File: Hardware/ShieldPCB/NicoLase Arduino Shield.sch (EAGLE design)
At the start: 19 parts, among them IC1 4050D, J1 ARDUINO_R3_SHIELD, U1 7432SE

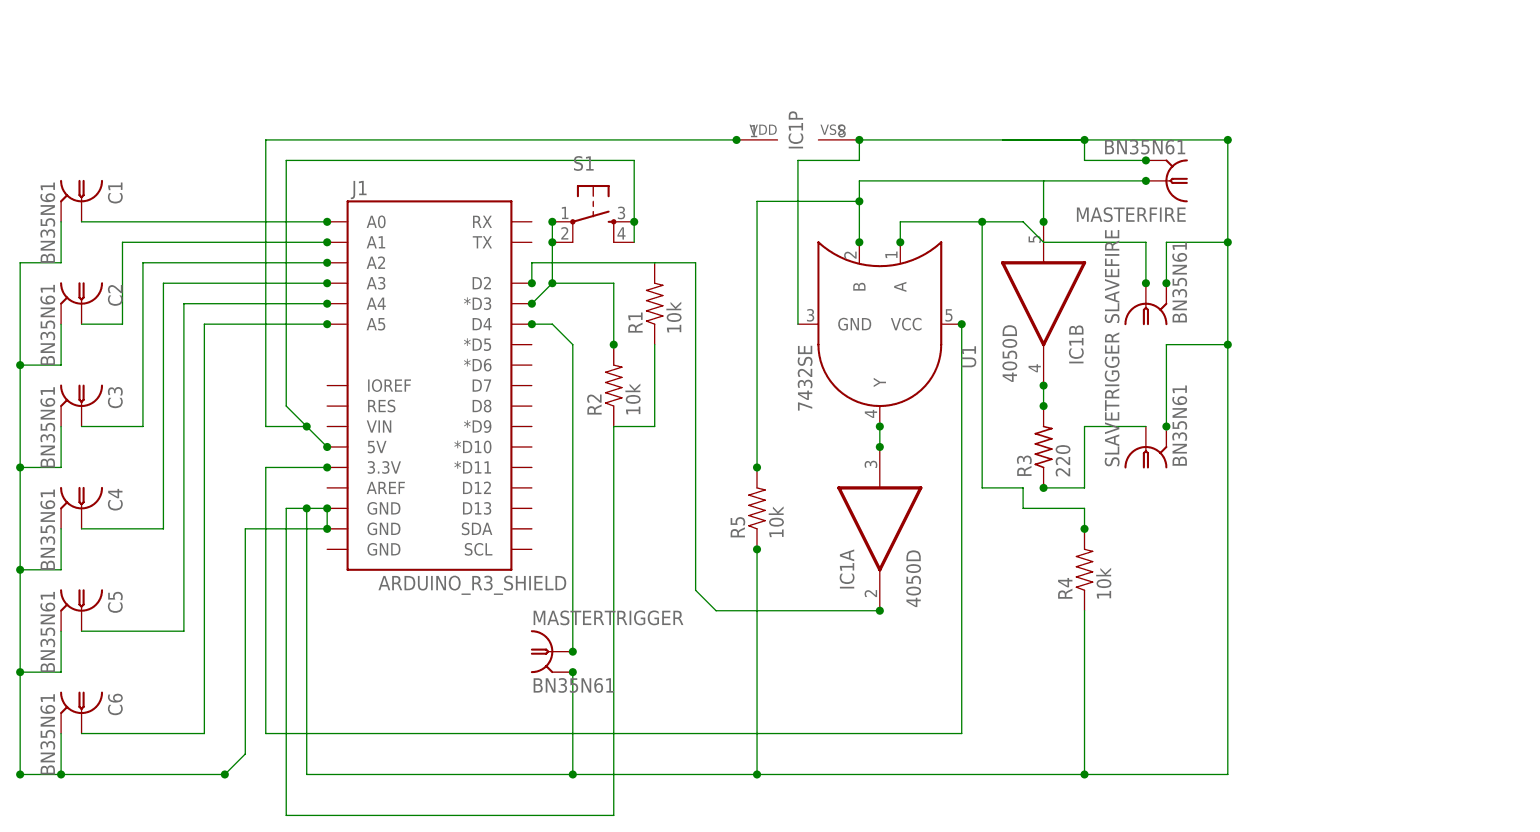
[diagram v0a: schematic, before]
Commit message: Added 0.1uF capacitors on power rails. Correcter minor schematic issues.
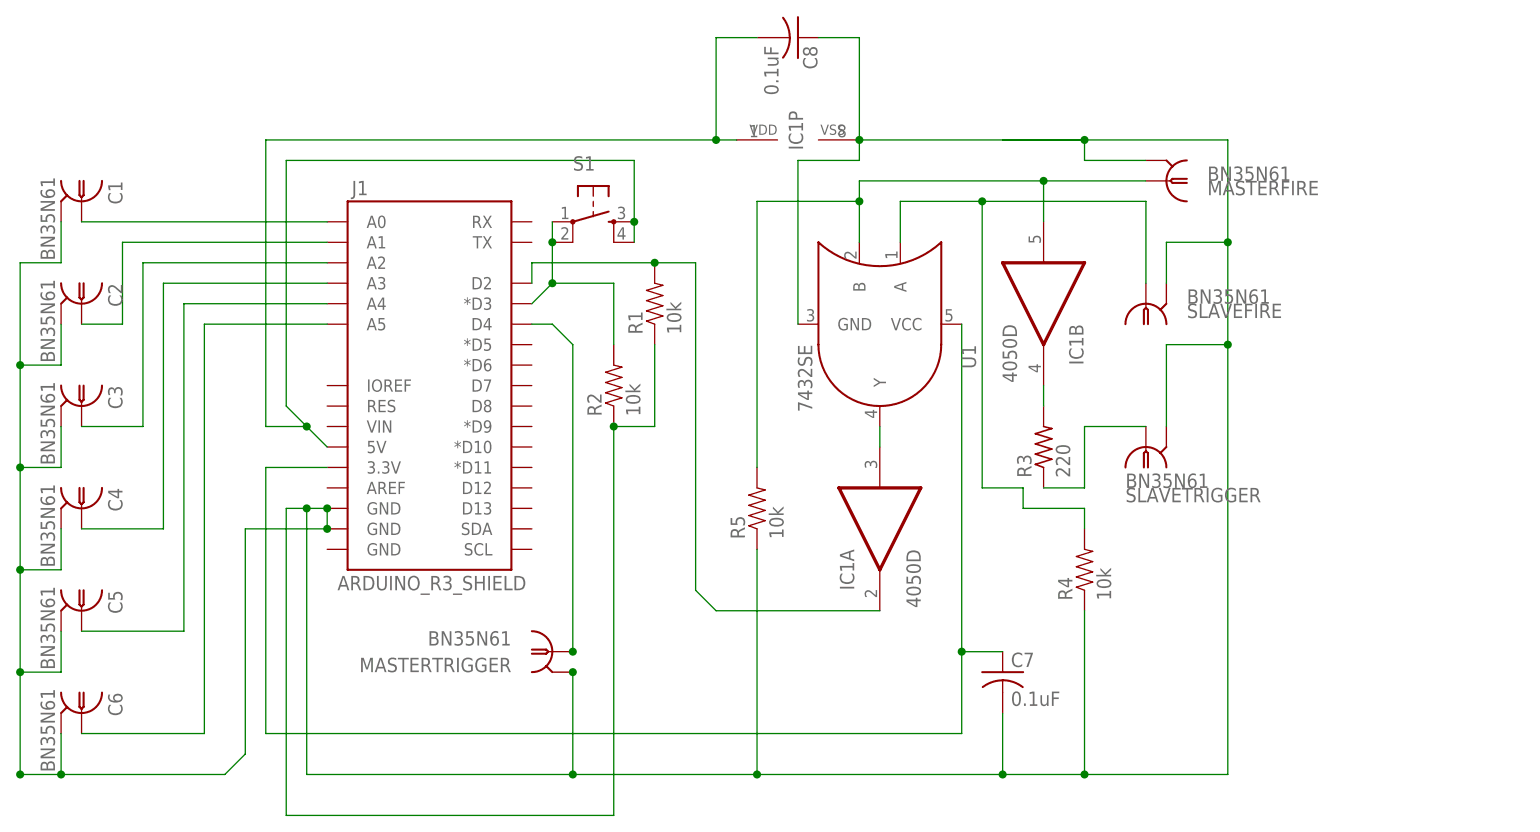
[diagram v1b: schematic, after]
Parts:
- added C7, C8: 0.1uF, rcl:C-USC1206
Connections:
- removed net N$2: C1.2, C2.2, C3.2, C4.2, C5.2, C6.2, IC1P.VSS, J1.GND@1, J1.GND@2, MASTERFIRE.2, MASTERTRIGGER.2, R1.1, R2.1, R4.1, R5.1, SLAVEFIRE.2, SLAVETRIGGER.2, U1.GND
- new net GND: C1.2, C2.2, C3.2, C4.2, C5.2, C6.2, C7.2, C8.1, IC1P.VSS, J1.GND@1, J1.GND@2, MASTERFIRE.2, MASTERTRIGGER.2, R1.1, R2.1, R4.1, R5.1, SLAVEFIRE.2, SLAVETRIGGER.2, U1.GND
- net N$1: now also C7.1
- net N$16: now also C8.2

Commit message: Review filcarv pull request.  Update silkscreen and README terminology for primary/secondary fire/trigger lines.
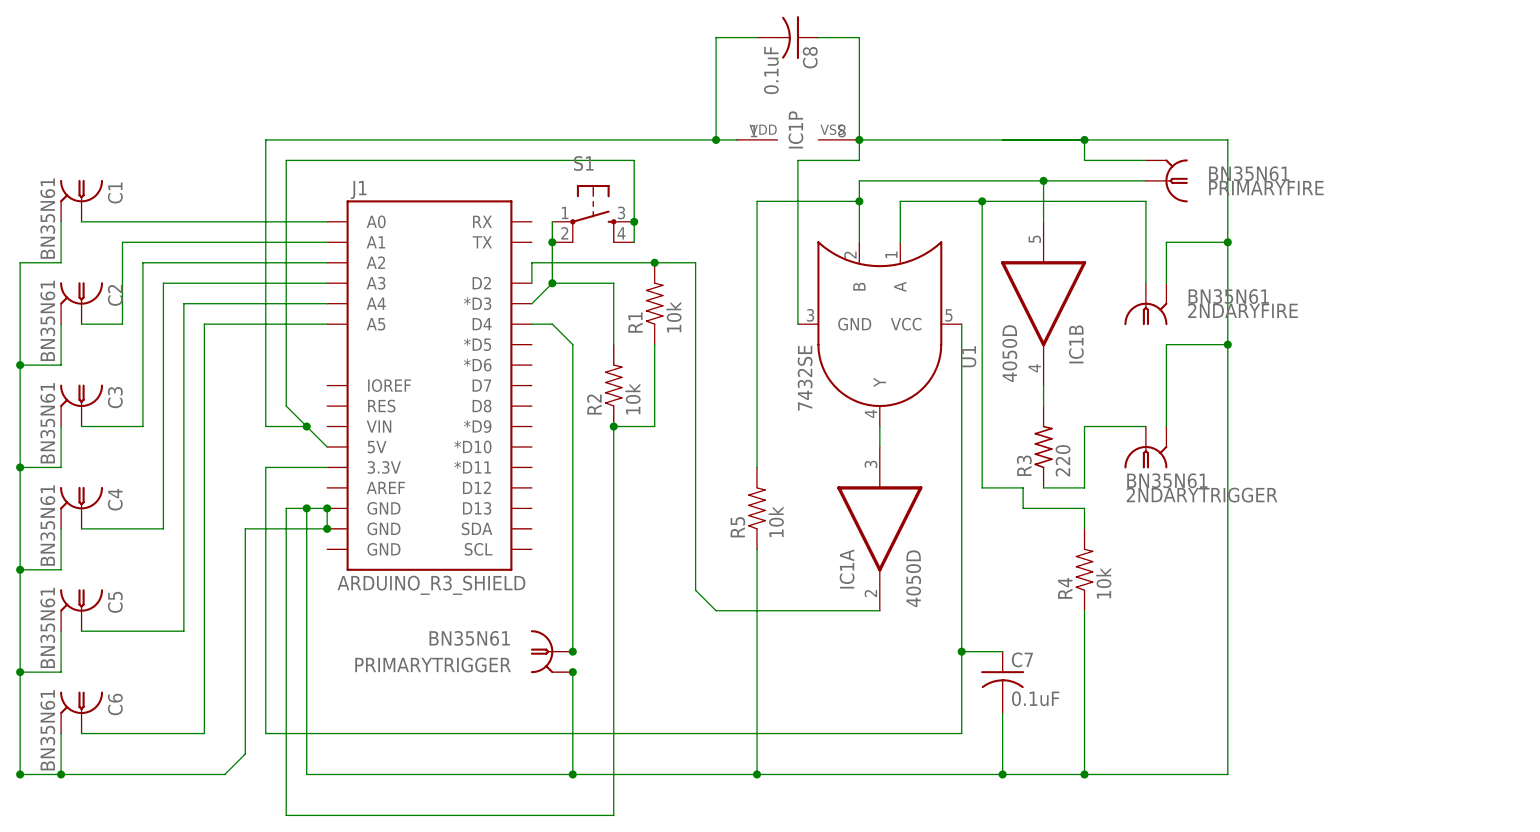
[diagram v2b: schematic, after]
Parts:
- renumbered MASTERFIRE to PRIMARYFIRE, MASTERTRIGGER to PRIMARYTRIGGER, SLAVEFIRE to 2NDARYFIRE, SLAVETRIGGER to 2NDARYTRIGGER
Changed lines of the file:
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@@
 <?xml version="1.0" encoding="utf-8"?>
 <!DOCTYPE eagle SYSTEM "eagle.dtd">
-<eagle version="9.5.1">
+<eagle version="9.0.1">
 <drawing>
 <settings>
@@
 <part name="IC1" library="40xx" deviceset="4050" device="D" value="4050D"/>
 <part name="C1" library="con-coax" deviceset="BN35N61" device=""/>
-<part name="MASTERFIRE" library="con-coax" deviceset="BN35N61" device=""/>
+<part name="PRIMARYFIRE" library="con-coax" deviceset="BN35N61" device=""/>
 <part name="C2" library="con-coax" deviceset="BN35N61" device=""/>
 <part name="C3" library="con-coax" deviceset="BN35N61" device=""/>
@@
 <part name="C5" library="con-coax" deviceset="BN35N61" device=""/>
 <part name="C6" library="con-coax" deviceset="BN35N61" device=""/>
-<part name="SLAVEFIRE" library="con-coax" deviceset="BN35N61" device=""/>
-<part name="SLAVETRIGGER" library="con-coax" deviceset="BN35N61" device=""/>
+<part name="2NDARYFIRE" library="con-coax" deviceset="BN35N61" device=""/>
+<part name="2NDARYTRIGGER" library="con-coax" deviceset="BN35N61" device=""/>
 <part name="U1" library="SparkFun-DigitalIC" deviceset="74*32" device="SE"/>
 <part name="R3" library="resistor" deviceset="R-US_" device="M1206" value="220"/>
-<part name="MASTERTRIGGER" library="con-coax" deviceset="BN35N61" device=""/>
+<part name="PRIMARYTRIGGER" library="con-coax" deviceset="BN35N61" device=""/>
 <part name="J1" library="SparkFun-Boards" deviceset="ARDUINO_R3_SHIELD" device=""/>
 <part name="R4" library="SparkFun-Resistors" deviceset="RESISTOR" device="1206" value="10k"/>
@@
 <attribute name="NAME" x="21.082" y="86.36" size="1.778" layer="95" rot="R270"/>
 </instance>
-<instance part="MASTERFIRE" gate="G$1" x="152.4" y="86.36" smashed="yes" rot="R180">
+<instance part="PRIMARYFIRE" gate="G$1" x="152.4" y="86.36" smashed="yes" rot="R180">
 <attribute name="VALUE" x="157.48" y="86.36" size="1.778" layer="96"/>
 <attribute name="NAME" x="157.48" y="84.582" size="1.778" layer="95"/>
@@
 <attribute name="NAME" x="21.082" y="22.86" size="1.778" layer="95" rot="R270"/>
 </instance>
-<instance part="SLAVEFIRE" gate="G$1" x="149.86" y="71.12" smashed="yes" rot="R90">
+<instance part="2NDARYFIRE" gate="G$1" x="149.86" y="71.12" smashed="yes" rot="R90">
 <attribute name="VALUE" x="154.94" y="71.12" size="1.778" layer="96"/>
 <attribute name="NAME" x="154.94" y="69.342" size="1.778" layer="95"/>
 </instance>
-<instance part="SLAVETRIGGER" gate="G$1" x="149.86" y="53.34" smashed="yes" rot="R90">
+<instance part="2NDARYTRIGGER" gate="G$1" x="149.86" y="53.34" smashed="yes" rot="R90">
 <attribute name="VALUE" x="147.32" y="48.26" size="1.778" layer="96"/>
 <attribute name="NAME" x="147.32" y="46.482" size="1.778" layer="95"/>
@@
 <attribute name="VALUE" x="140.462" y="49.53" size="1.778" layer="96" rot="R90"/>
 </instance>
-<instance part="MASTERTRIGGER" gate="G$1" x="76.2" y="27.94" smashed="yes">
+<instance part="PRIMARYTRIGGER" gate="G$1" x="76.2" y="27.94" smashed="yes">
 <attribute name="VALUE" x="71.12" y="30.48" size="1.778" layer="96" rot="R180"/>
 <attribute name="NAME" x="71.12" y="27.178" size="1.778" layer="95" rot="R180"/>
@@
 <wire x1="101.6" y1="83.82" x2="101.6" y2="50.8" width="0.1524" layer="91"/>
 <junction x="114.3" y="83.82"/>
-<pinref part="MASTERFIRE" gate="G$1" pin="1"/>
+<pinref part="PRIMARYFIRE" gate="G$1" pin="1"/>
 <wire x1="149.86" y1="86.36" x2="137.16" y2="86.36" width="0.1524" layer="91"/>
 <pinref part="IC1" gate="B" pin="I"/>
@@
 <pinref part="IC1" gate="P" pin="VSS"/>
 <junction x="114.3" y="91.44"/>
-<pinref part="SLAVETRIGGER" gate="G$1" pin="2"/>
+<pinref part="2NDARYTRIGGER" gate="G$1" pin="2"/>
 <wire x1="152.4" y1="66.04" x2="152.4" y2="55.88" width="0.1524" layer="91"/>
-<pinref part="SLAVEFIRE" gate="G$1" pin="2"/>
+<pinref part="2NDARYFIRE" gate="G$1" pin="2"/>
 <wire x1="152.4" y1="78.74" x2="152.4" y2="73.66" width="0.1524" layer="91"/>
-<pinref part="MASTERFIRE" gate="G$1" pin="2"/>
+<pinref part="PRIMARYFIRE" gate="G$1" pin="2"/>
 <wire x1="149.86" y1="88.9" x2="142.24" y2="88.9" width="0.1524" layer="91"/>
 <wire x1="142.24" y1="88.9" x2="142.24" y2="91.44" width="0.1524" layer="91"/>
@@
 <wire x1="38.1" y1="15.24" x2="35.56" y2="12.7" width="0.1524" layer="91"/>
 <wire x1="48.26" y1="45.72" x2="48.26" y2="43.18" width="0.1524" layer="91"/>
-<pinref part="MASTERTRIGGER" gate="G$1" pin="2"/>
+<pinref part="PRIMARYTRIGGER" gate="G$1" pin="2"/>
 <wire x1="78.74" y1="25.4" x2="78.74" y2="12.7" width="0.1524" layer="91"/>
 <junction x="78.74" y="25.4"/>
@@
 <net name="N$11" class="0">
 <segment>
-<pinref part="SLAVETRIGGER" gate="G$1" pin="1"/>
+<pinref part="2NDARYTRIGGER" gate="G$1" pin="1"/>
 <wire x1="149.86" y1="55.88" x2="142.24" y2="55.88" width="0.1524" layer="91"/>
 <pinref part="R3" gate="G$1" pin="1"/>
@@
 <wire x1="76.2" y1="68.58" x2="78.74" y2="66.04" width="0.1524" layer="91"/>
 <wire x1="78.74" y1="66.04" x2="78.74" y2="27.94" width="0.1524" layer="91"/>
-<pinref part="MASTERTRIGGER" gate="G$1" pin="1"/>
+<pinref part="PRIMARYTRIGGER" gate="G$1" pin="1"/>
 <pinref part="J1" gate="G$1" pin="D4"/>
 <wire x1="76.2" y1="68.58" x2="73.66" y2="68.58" width="0.1524" layer="91"/>
@@
 <wire x1="134.62" y1="48.26" x2="134.62" y2="45.72" width="0.1524" layer="91"/>
 <wire x1="129.54" y1="48.26" x2="134.62" y2="48.26" width="0.1524" layer="91"/>
-<pinref part="SLAVEFIRE" gate="G$1" pin="1"/>
+<pinref part="2NDARYFIRE" gate="G$1" pin="1"/>
 <wire x1="149.86" y1="73.66" x2="149.86" y2="83.82" width="0.1524" layer="91"/>
 <wire x1="149.86" y1="83.82" x2="129.54" y2="83.82" width="0.1524" layer="91"/>

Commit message: Grounded the non-used gates.
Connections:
- net GND: now also IC1C.I, IC1D.I, IC1E.I, IC1F.I
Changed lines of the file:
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@@
 <?xml version="1.0" encoding="utf-8"?>
 <!DOCTYPE eagle SYSTEM "eagle.dtd">
-<eagle version="9.0.1">
+<eagle version="9.5.1">
 <drawing>
 <settings>
@@
 <attribute name="VALUE" x="102.489" y="103.124" size="1.778" layer="96" rot="R270"/>
 </instance>
+<instance part="IC1" gate="C" x="185.42" y="55.88" smashed="yes">
+<attribute name="NAME" x="187.96" y="59.055" size="1.778" layer="95"/>
+<attribute name="VALUE" x="187.96" y="50.8" size="1.778" layer="96"/>
+</instance>
+<instance part="IC1" gate="D" x="185.42" y="43.18" smashed="yes">
+<attribute name="NAME" x="187.96" y="46.355" size="1.778" layer="95"/>
+<attribute name="VALUE" x="187.96" y="38.1" size="1.778" layer="96"/>
+</instance>
+<instance part="IC1" gate="E" x="185.42" y="30.48" smashed="yes">
+<attribute name="NAME" x="187.96" y="33.655" size="1.778" layer="95"/>
+<attribute name="VALUE" x="187.96" y="25.4" size="1.778" layer="96"/>
+</instance>
+<instance part="IC1" gate="F" x="185.42" y="17.78" smashed="yes">
+<attribute name="NAME" x="187.96" y="20.955" size="1.778" layer="95"/>
+<attribute name="VALUE" x="187.96" y="12.7" size="1.778" layer="96"/>
+</instance>
 </instances>
 <busses>
@@
 <wire x1="109.22" y1="104.14" x2="114.3" y2="104.14" width="0.1524" layer="91"/>
 <wire x1="114.3" y1="104.14" x2="114.3" y2="91.44" width="0.1524" layer="91"/>
+<wire x1="160.02" y1="12.7" x2="172.72" y2="12.7" width="0.1524" layer="91"/>
+<junction x="160.02" y="12.7"/>
+<pinref part="IC1" gate="C" pin="I"/>
+<wire x1="172.72" y1="12.7" x2="172.72" y2="17.78" width="0.1524" layer="91"/>
+<wire x1="172.72" y1="17.78" x2="172.72" y2="30.48" width="0.1524" layer="91"/>
+<wire x1="172.72" y1="30.48" x2="172.72" y2="43.18" width="0.1524" layer="91"/>
+<wire x1="172.72" y1="43.18" x2="172.72" y2="55.88" width="0.1524" layer="91"/>
+<wire x1="172.72" y1="55.88" x2="175.26" y2="55.88" width="0.1524" layer="91"/>
+<pinref part="IC1" gate="D" pin="I"/>
+<wire x1="175.26" y1="43.18" x2="172.72" y2="43.18" width="0.1524" layer="91"/>
+<junction x="172.72" y="43.18"/>
+<pinref part="IC1" gate="E" pin="I"/>
+<wire x1="175.26" y1="30.48" x2="172.72" y2="30.48" width="0.1524" layer="91"/>
+<junction x="172.72" y="30.48"/>
+<pinref part="IC1" gate="F" pin="I"/>
+<wire x1="175.26" y1="17.78" x2="172.72" y2="17.78" width="0.1524" layer="91"/>
+<junction x="172.72" y="17.78"/>
 </segment>
 </net>
